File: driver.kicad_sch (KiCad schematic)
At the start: 38 parts, among them Q4 SIZ322DT, Q5 SIZ322DT, Q6 SIZ322DT, U4 TMC6200

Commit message: Cleanup part properties.
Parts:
- Q4, Q5, Q6: Arrow Part Number SIZ322DT-T1-GE3 -> (none); Arrow Price/Stock https://www.arrow.com/en/products/siz322dt-t1-ge3/vishay -> (none); Height 0.8 -> (none); Manufacturer_Name Vishay -> (none); Mouser Part Number 78-SIZ322DT-T1-GE3 -> (none); Mouser Price/Stock https://www.mouser.co.uk/ProductDetail/Vishay-Siliconix/SIZ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 -> (none)
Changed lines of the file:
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@@
-      (effects (font (size 1.27 1.27)) (justify left top) hide)
-    )
-    (property "Height" "0.8" (at 246.38 529.54 0)
-      (effects (font (size 1.27 1.27)) (justify left top) hide)
-    )
-    (property "Manufacturer_Name" "Vishay" (at 246.38 629.54 0)
-      (effects (font (size 1.27 1.27)) (justify left top) hide)
-    )
-    (property "Manufacturer_Part_Number" "" (at 246.38 729.54 0)
-      (effects (font (size 1.27 1.27)) (justify left top) hide)
-    )
-    (property "Mouser Part Number" "78-SIZ322DT-T1-GE3" (at 246.38 829.54 0)
-      (effects (font (size 1.27 1.27)) (justify left top) hide)
-    )
-    (property "Mouser Price/Stock" "https://www.mouser.co.uk/ProductDetail/Vishay-Siliconix/SIZ322DT-T1-GE3?qs=7EBvPakHacV23cS55WZm1Q%3D%3D" (at 246.38 929.54 0)
-      (effects (font (size 1.27 1.27)) (justify left top) hide)
-    )
-    (property "Arrow Part Number" "SIZ322DT-T1-GE3" (at 246.38 1029.54 0)
-      (effects (font (size 1.27 1.27)) (justify left top) hide)
-    )
-    (property "Arrow Price/Stock" "https://www.arrow.com/en/products/siz322dt-t1-ge3/vishay" (at 246.38 1129.54 0)
       (effects (font (size 1.27 1.27)) (justify left top) hide)
     )
@@
       (effects (font (size 1.27 1.27)) (justify left top) hide)
     )
-    (property "Height" "0.8" (at 246.38 433.02 0)
-      (effects (font (size 1.27 1.27)) (justify left top) hide)
-    )
-    (property "Manufacturer_Name" "Vishay" (at 246.38 533.02 0)
-      (effects (font (size 1.27 1.27)) (justify left top) hide)
-    )
-    (property "Manufacturer_Part_Number" "" (at 246.38 633.02 0)
-      (effects (font (size 1.27 1.27)) (justify left top) hide)
-    )
-    (property "Mouser Part Number" "78-SIZ322DT-T1-GE3" (at 246.38 733.02 0)
-      (effects (font (size 1.27 1.27)) (justify left top) hide)
-    )
-    (property "Mouser Price/Stock" "https://www.mouser.co.uk/ProductDetail/Vishay-Siliconix/SIZ322DT-T1-GE3?qs=7EBvPakHacV23cS55WZm1Q%3D%3D" (at 246.38 833.02 0)
-      (effects (font (size 1.27 1.27)) (justify left top) hide)
-    )
-    (property "Arrow Part Number" "SIZ322DT-T1-GE3" (at 246.38 933.02 0)
-      (effects (font (size 1.27 1.27)) (justify left top) hide)
-    )
-    (property "Arrow Price/Stock" "https://www.arrow.com/en/products/siz322dt-t1-ge3/vishay" (at 246.38 1033.02 0)
-      (effects (font (size 1.27 1.27)) (justify left top) hide)
-    )
     (property "MPN" "SIZ322DT-T1-GE3" (at 219.71 38.1 0)
       (effects (font (size 1.27 1.27)) hide)
@@
       (effects (font (size 1.27 1.27)) (justify left top) hide)
     )
-    (property "Height" "0.8" (at 246.38 481.28 0)
-      (effects (font (size 1.27 1.27)) (justify left top) hide)
-    )
-    (property "Manufacturer_Name" "Vishay" (at 246.38 581.28 0)
-      (effects (font (size 1.27 1.27)) (justify left top) hide)
-    )
-    (property "Manufacturer_Part_Number" "" (at 246.38 681.28 0)
-      (effects (font (size 1.27 1.27)) (justify left top) hide)
-    )
-    (property "Mouser Part Number" "78-SIZ322DT-T1-GE3" (at 246.38 781.28 0)
-      (effects (font (size 1.27 1.27)) (justify left top) hide)
-    )
-    (property "Mouser Price/Stock" "https://www.mouser.co.uk/ProductDetail/Vishay-Siliconix/SIZ322DT-T1-GE3?qs=7EBvPakHacV23cS55WZm1Q%3D%3D" (at 246.38 881.28 0)
-      (effects (font (size 1.27 1.27)) (justify left top) hide)
-    )
-    (property "Arrow Part Number" "SIZ322DT-T1-GE3" (at 246.38 981.28 0)
-      (effects (font (size 1.27 1.27)) (justify left top) hide)
-    )
-    (property "Arrow Price/Stock" "https://www.arrow.com/en/products/siz322dt-t1-ge3/vishay" (at 246.38 1081.28 0)
-      (effects (font (size 1.27 1.27)) (justify left top) hide)
-    )

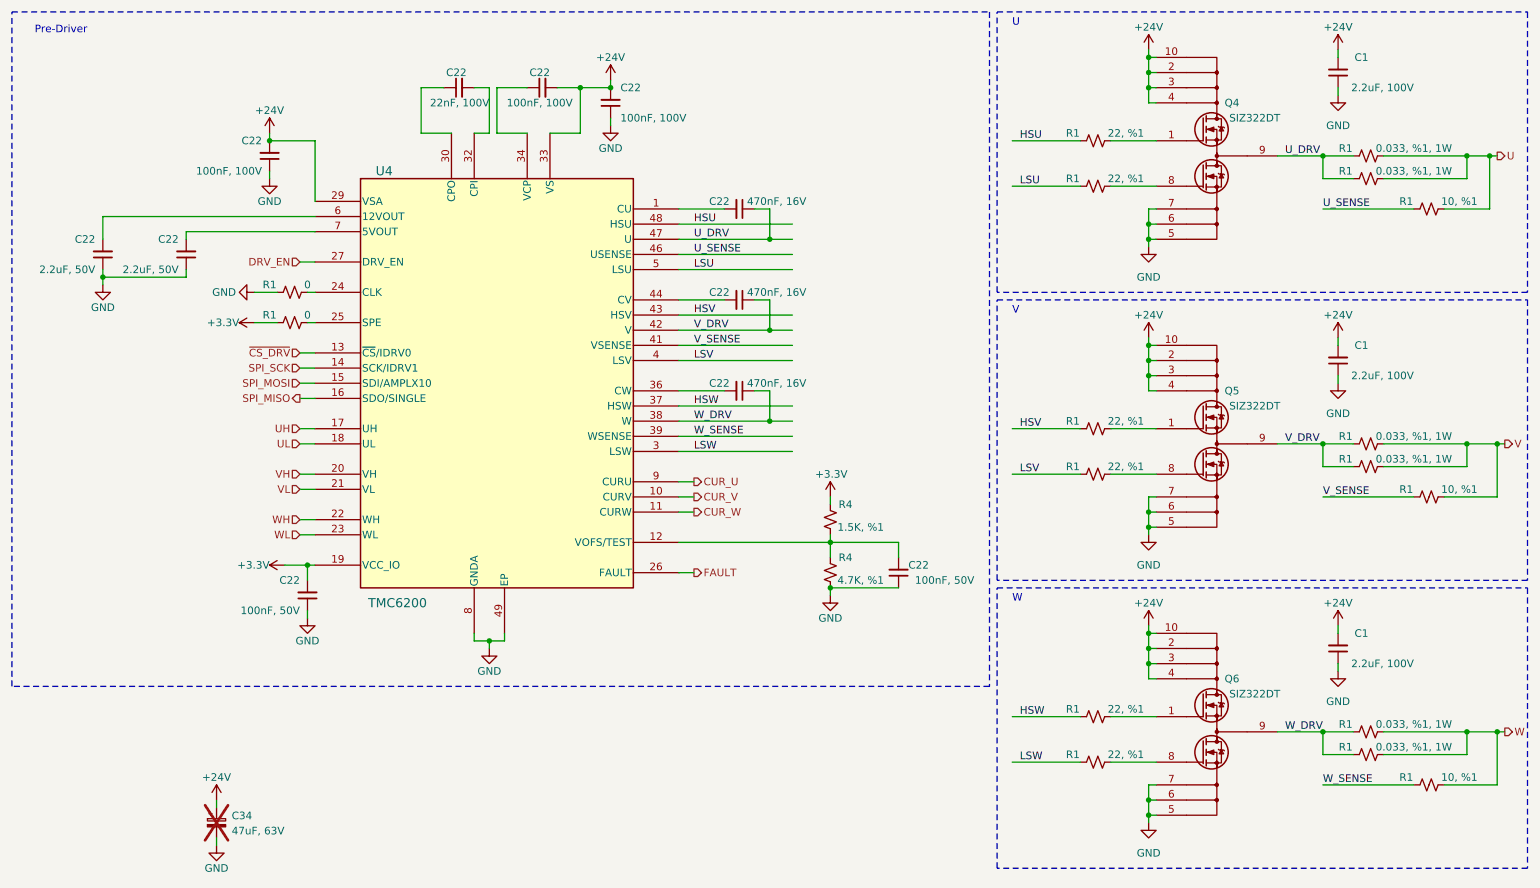
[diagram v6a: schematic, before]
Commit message: Fix issues found during the test, in the schematics.
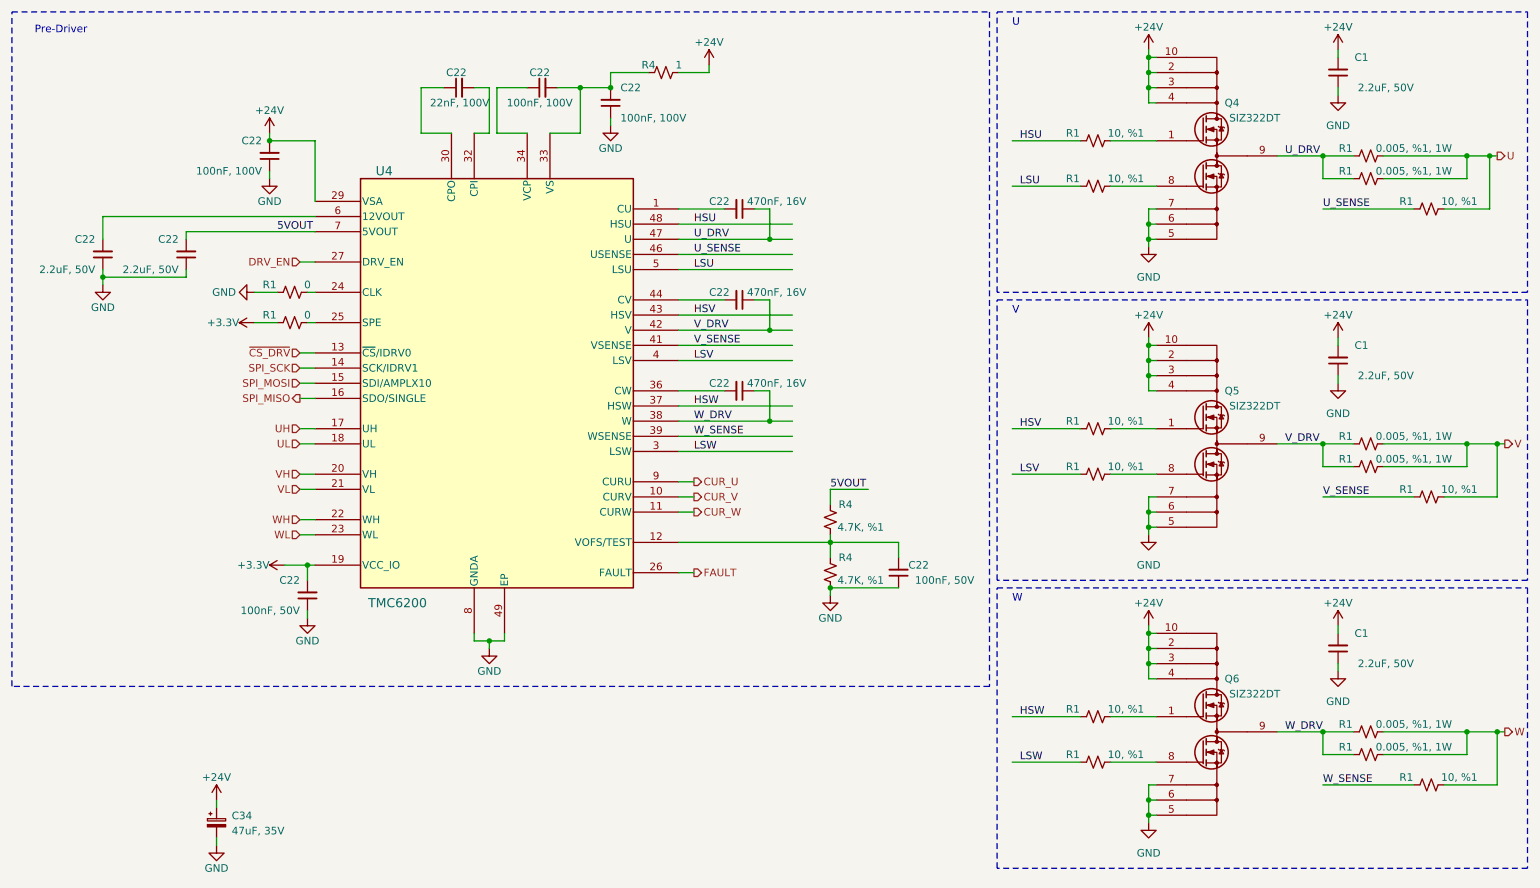
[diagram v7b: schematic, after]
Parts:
- removed R4: 1.5K, %1, Resistor_SMD:R_0402_1005Metric, symbol Device:R_Small_US
- added R4: 4.7K, %1, Resistor_SMD:R_0402_1005Metric, symbol Device:R_Small_US
- added R4: 1, Resistor_SMD:R_0402_1005Metric, symbol Device:R_Small_US
- C1: value 2.2uF, 100V -> 2.2uF, 50V; MPN CL31B225KCHSNNE -> CL31B225KBHNNNE
- C34: value 47uF, 63V -> 47uF, 35V; MPN 865080645012 -> 865080543009; now fitted
- R1: value 22, %1 -> 10, %1; MPN ERJ-2RKF22R0X -> ERJ-2RKF10R0X
- R1: value 0.033, %1, 1W -> 0.005, %1, 1W; MPN ERJ-8CWFR033V -> CFN1206-FX-R005ELF
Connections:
- net +24V: now also R4.1; no longer C22.2, C22.2, U4.33 (VS)
- net at C22.2, R4.2, U4.12 (VOFS/TEST): now also R4.1
- net 5VOUT: now reaches C22.2, U4.7 (5VOUT)
- net 5VOUT: now also R4.2
- new net: C22.2, C22.2, R4.2, U4.33 (VS)

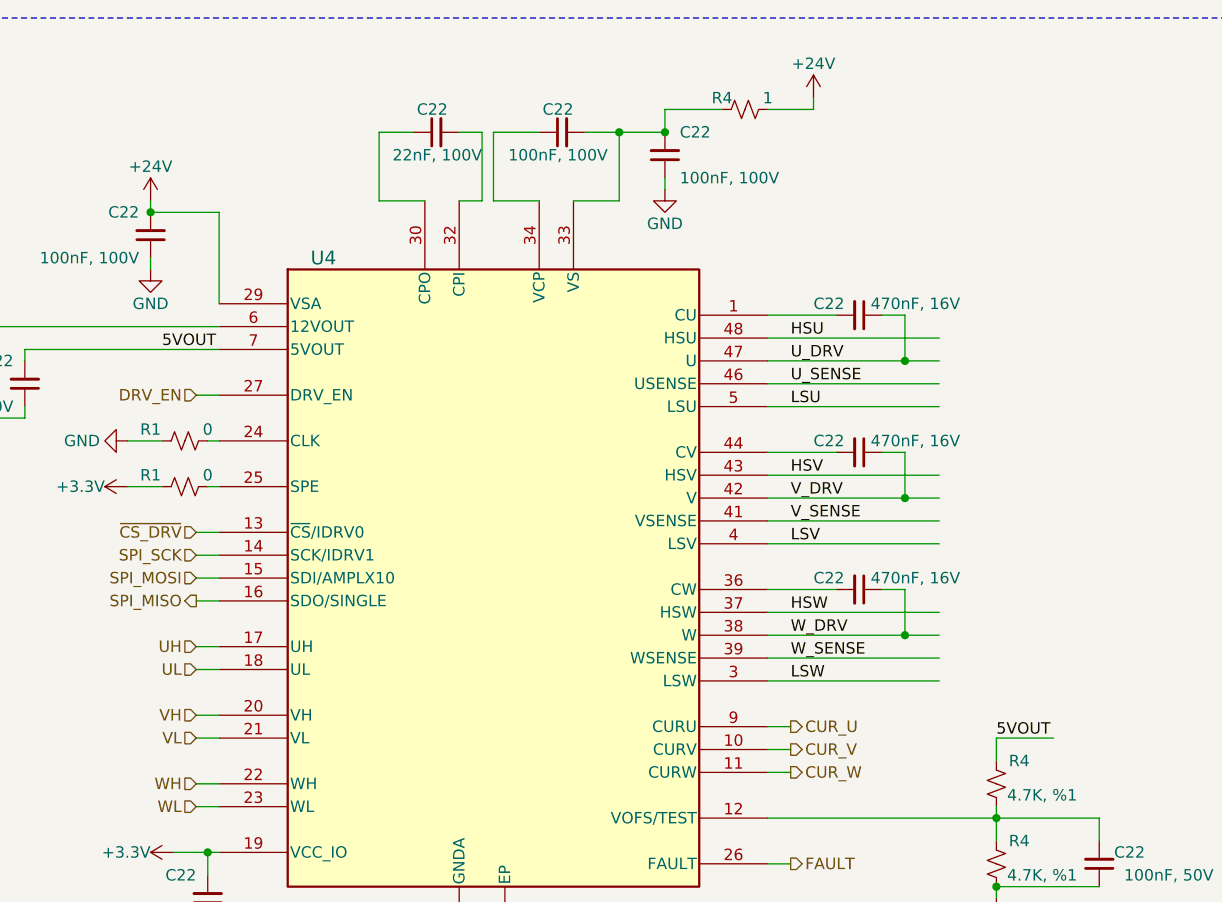
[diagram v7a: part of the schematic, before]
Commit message: Applied the fixes to the pcb.
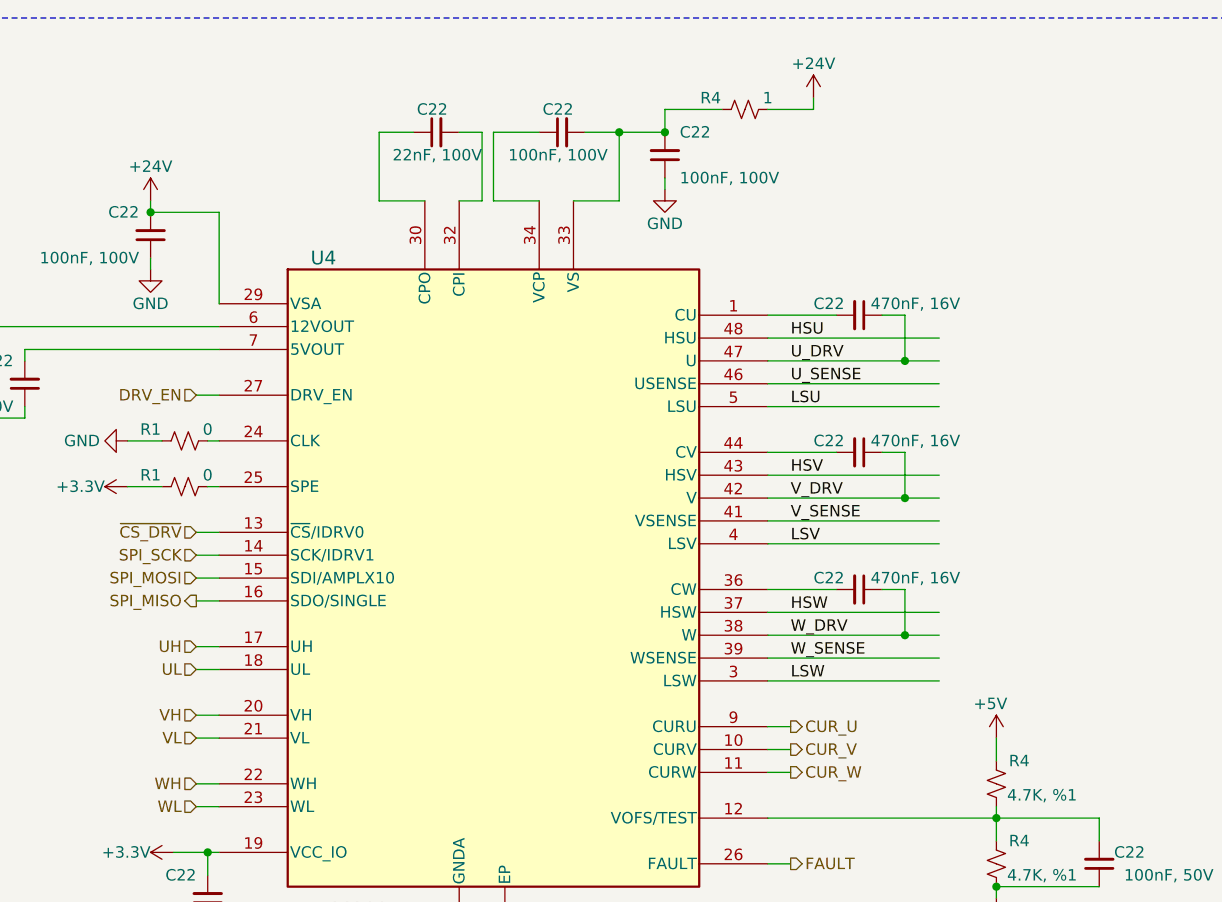
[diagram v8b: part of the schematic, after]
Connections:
- net 5VOUT: no longer names the net of C22.2, U4.7 (5VOUT)
- net 5VOUT: no longer R4.2
- new net +5V: R4.2
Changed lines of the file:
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@@
-    (stroke (width 0) (type default))
-  )
-  (wire (pts (xy 154.94 95.25) (xy 161.29 95.25))
     (stroke (width 0) (type default))
   )
@@
     (effects (font (size 1.27 1.27)) (justify left bottom))
   )
-  (label "5VOUT" (at 154.94 95.25 0) (fields_autoplaced)
-    (effects (font (size 1.27 1.27)) (justify left bottom))
-  )
   (label "HSU" (at 132.08 50.8 0) (fields_autoplaced)
     (effects (font (size 1.27 1.27)) (justify left bottom))
@@
   )
   (label "V_DRV" (at 231.14 87.63 0) (fields_autoplaced)
-    (effects (font (size 1.27 1.27)) (justify left bottom))
-  )
-  (label "5VOUT" (at 62.23 52.07 0) (fields_autoplaced)
     (effects (font (size 1.27 1.27)) (justify left bottom))
   )
@@
   (symbol (lib_id "Device:R_Small_US") (at 127 25.4 270) (unit 1)
     (in_bom yes) (on_board yes) (dnp no)
-    (property "Reference" "R4" (at 124.46 24.13 90)
+    (property "Reference" "R4" (at 123.19 24.13 90)
       (effects (font (size 1.27 1.27)))
     )
@@
         )
       )
+    )
+  )
+  (symbol (lib_id "power:+5V") (at 154.94 95.25 0) (unit 1)
+    (in_bom yes) (on_board yes) (dnp no)
+    (property "Reference" "#PWR012" (at 154.94 99.06 0)
+      (effects (font (size 1.27 1.27)) hide)
+    )
+    (property "Value" "+5V" (at 152.4 91.44 0)
+      (effects (font (size 1.27 1.27)) (justify left))
+    )
+    (property "Footprint" "" (at 154.94 95.25 0)
+      (effects (font (size 1.27 1.27)) hide)
+    )
+    (property "Datasheet" "" (at 154.94 95.25 0)
+      (effects (font (size 1.27 1.27)) hide)
+    )
+    (pin "1")
+    (instances
+      (project "motor-driver"
+        (path "/314549f2-cc46-4559-991a-ae9411f3d209/25794513-4b05-4cf2-b97c-a9dcfa280e83"
+          (reference "#PWR012") (unit 1)
+        )
+        (path "/314549f2-cc46-4559-991a-ae9411f3d209/ffb80554-b8ca-4e0c-96b9-7870843c432f"
+          (reference "#PWR047") (unit 1)
+        )
+      )
